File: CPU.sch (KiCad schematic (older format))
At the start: 14 parts, among them J10 SWD, U1 STM32F405RGTx, Y1 8MHz

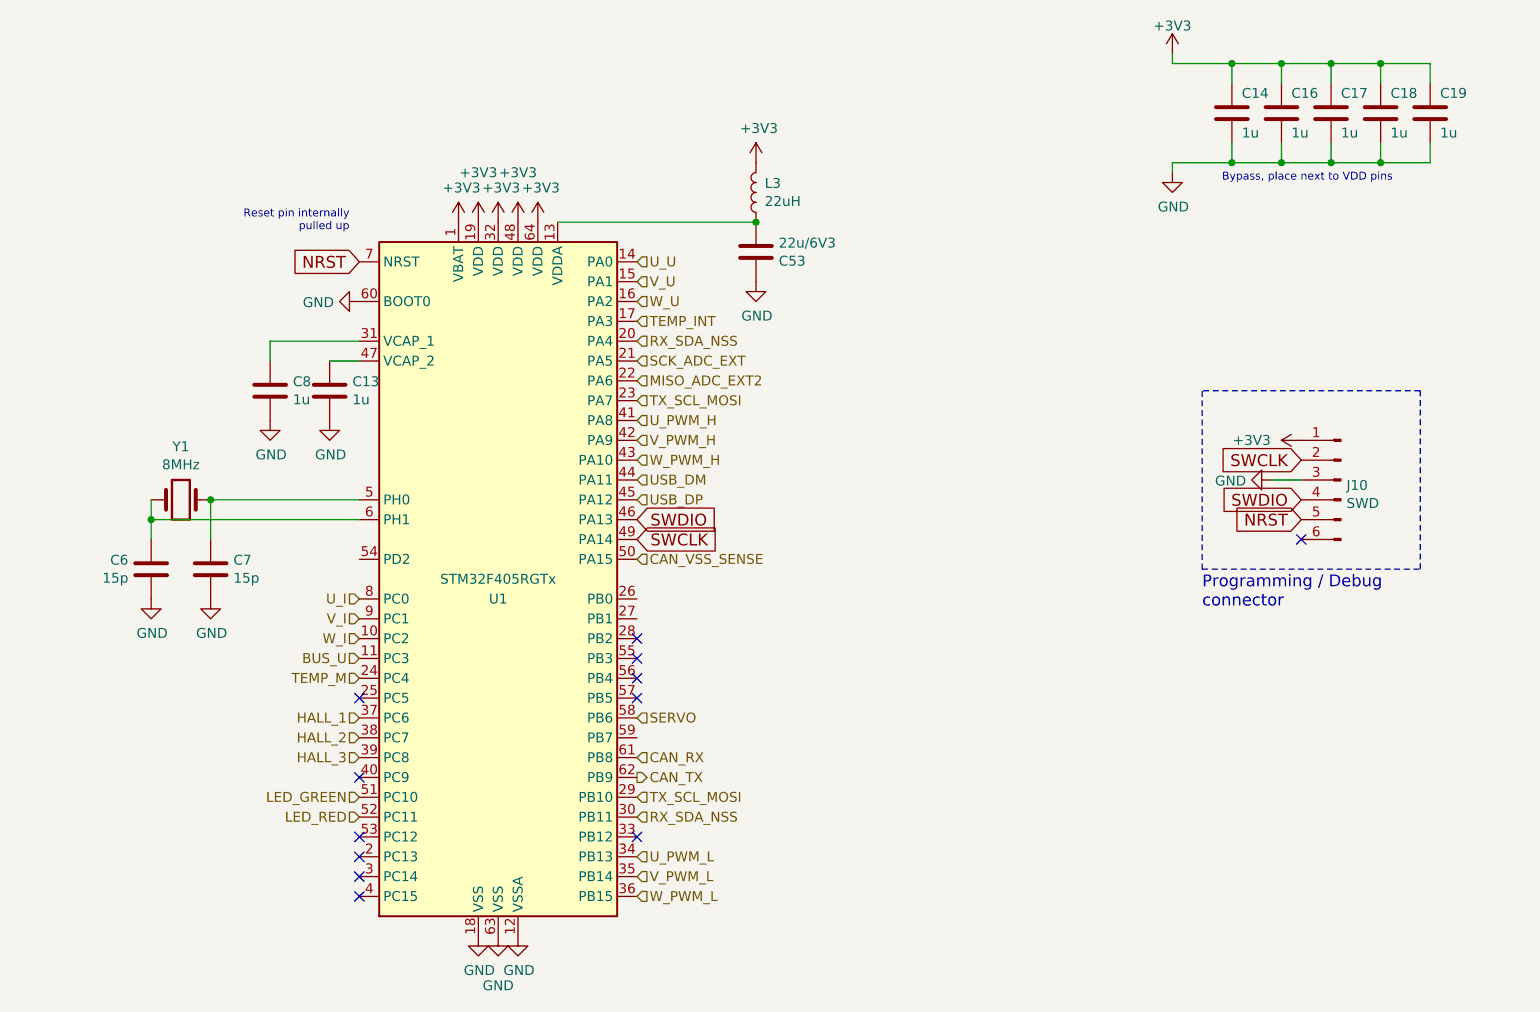
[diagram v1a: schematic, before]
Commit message: - changed CSA for Hall effect sensors - updated power stage layout
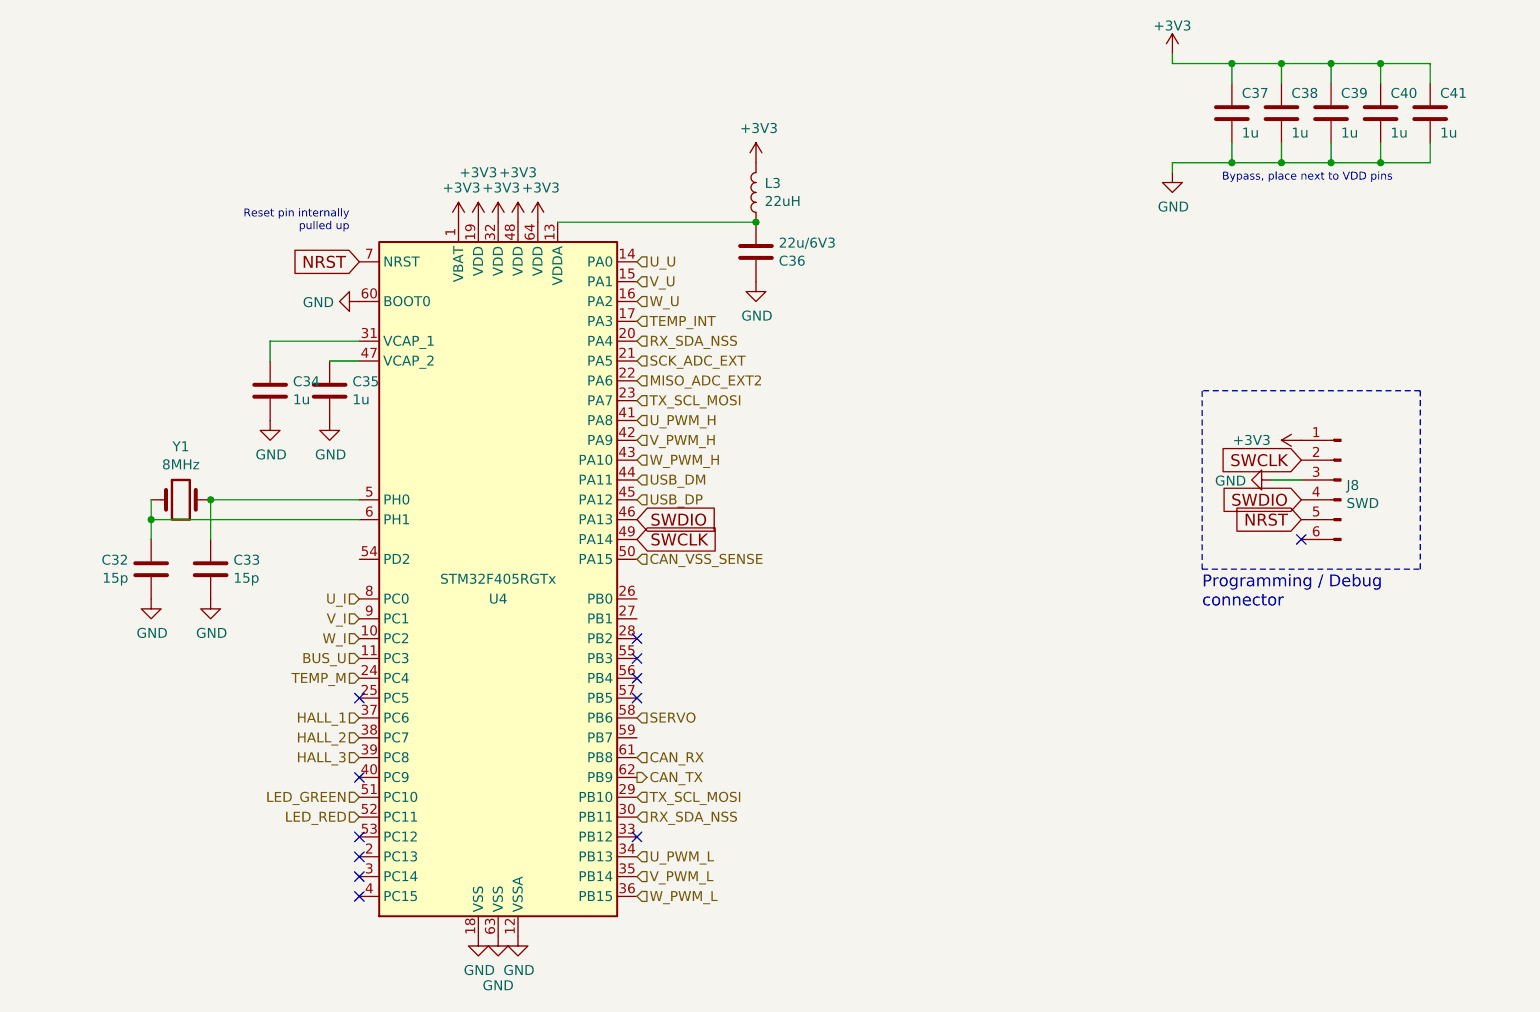
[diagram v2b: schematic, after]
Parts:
- renumbered C6 to C32, C7 to C33, C8 to C34, C13 to C35, C53 to C36, C14 to C37, C16 to C38, C17 to C39, C18 to C40, C19 to C41, J10 to J8, U1 to U4
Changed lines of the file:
@@
 Bypass, place next to VDD pins
 $Comp
-L HSWR-V2-rescue:+3V3-power #PWR050
+L HSWR-V2-rescue:+3V3-power #PWR082
 U 1 1 5752A907
 P 9750 2900
-F 0 "#PWR050" H 9750 2750 50  0001 C CNN
+F 0 "#PWR082" H 9750 2750 50  0001 C CNN
 F 1 "+3V3" V 9750 3150 50  0000 C CNN
 F 2 "" H 9750 2900 50  0000 C CNN
@@
 $EndComp
 $Comp
-L HSWR-V2-rescue:+3V3-power #PWR051
+L HSWR-V2-rescue:+3V3-power #PWR079
 U 1 1 5752A9C6
 P 9100 950
-F 0 "#PWR051" H 9100 800 50  0001 C CNN
+F 0 "#PWR079" H 9100 800 50  0001 C CNN
 F 1 "+3V3" H 9100 1090 50  0000 C CNN
 F 2 "" H 9100 950 50  0000 C CNN
@@
 NoConn ~ 5000 5200
 $Comp
-L HSWR-V2-rescue:C-Device C13
+L HSWR-V2-rescue:C-Device C35
 U 1 1 5CA0C3E8
 P 4850 2650
-F 0 "C13" H 4965 2696 50  0000 L CNN
+F 0 "C35" H 4965 2696 50  0000 L CNN
 F 1 "1u" H 4965 2605 50  0000 L CNN
 F 2 "Capacitor_SMD:C_0805_2012Metric" H 4888 2500 50  0001 C CNN
@@
 $EndComp
 $Comp
-L HSWR-V2-rescue:C-Device C8
+L HSWR-V2-rescue:C-Device C34
 U 1 1 5CA0C416
 P 4550 2650
-F 0 "C8" H 4665 2696 50  0000 L CNN
+F 0 "C34" H 4665 2696 50  0000 L CNN
 F 1 "1u" H 4665 2605 50  0000 L CNN
 F 2 "Capacitor_SMD:C_0805_2012Metric" H 4588 2500 50  0001 C CNN
@@
 	4550 2400 4550 2500
 $Comp
-L HSWR-V2-rescue:GND-power #PWR0123
+L HSWR-V2-rescue:GND-power #PWR066
 U 1 1 5CA0EB5F
 P 4550 2800
-F 0 "#PWR0123" H 4550 2550 50  0001 C CNN
+F 0 "#PWR066" H 4550 2550 50  0001 C CNN
 F 1 "GND" H 4555 2627 50  0000 C CNN
 F 2 "" H 4550 2800 50  0001 C CNN
@@
 $EndComp
 $Comp
-L HSWR-V2-rescue:GND-power #PWR0124
+L HSWR-V2-rescue:GND-power #PWR067
 U 1 1 5CA0EB79
 P 4850 2800
-F 0 "#PWR0124" H 4850 2550 50  0001 C CNN
+F 0 "#PWR067" H 4850 2550 50  0001 C CNN
 F 1 "GND" H 4855 2627 50  0000 C CNN
 F 2 "" H 4850 2800 50  0001 C CNN
@@
 $EndComp
 $Comp
-L HSWR-V2-rescue:GND-power #PWR0125
+L HSWR-V2-rescue:GND-power #PWR068
 U 1 1 5CA0EDF0
 P 5000 2200
-F 0 "#PWR0125" H 5000 1950 50  0001 C CNN
+F 0 "#PWR068" H 5000 1950 50  0001 C CNN
 F 1 "GND" V 5005 2072 50  0000 R CNN
 F 2 "" H 5000 2200 50  0001 C CNN
@@
 $EndComp
 $Comp
-L HSWR-V2-rescue:C-Device C7
+L HSWR-V2-rescue:C-Device C33
 U 1 1 5CA0F099
 P 4250 3550
-F 0 "C7" H 4365 3596 50  0000 L CNN
+F 0 "C33" H 4365 3596 50  0000 L CNN
 F 1 "15p" H 4365 3505 50  0000 L CNN
 F 2 "Capacitor_SMD:C_0805_2012Metric" H 4288 3400 50  0001 C CNN
@@
 $EndComp
 $Comp
-L HSWR-V2-rescue:GND-power #PWR0126
+L HSWR-V2-rescue:GND-power #PWR065
 U 1 1 5CA0F12A
 P 4250 3700
-F 0 "#PWR0126" H 4250 3450 50  0001 C CNN
+F 0 "#PWR065" H 4250 3450 50  0001 C CNN
 F 1 "GND" H 4255 3527 50  0000 C CNN
 F 2 "" H 4250 3700 50  0001 C CNN
@@
 $EndComp
 $Comp
-L HSWR-V2-rescue:C-Device C6
+L HSWR-V2-rescue:C-Device C32
 U 1 1 5CA0F13F
 P 3950 3550
-F 0 "C6" H 3835 3504 50  0000 R CNN
+F 0 "C32" H 3835 3504 50  0000 R CNN
 F 1 "15p" H 3835 3595 50  0000 R CNN
 F 2 "Capacitor_SMD:C_0805_2012Metric" H 3988 3400 50  0001 C CNN
@@
 $EndComp
 $Comp
-L HSWR-V2-rescue:GND-power #PWR0127
+L HSWR-V2-rescue:GND-power #PWR064
 U 1 1 5CA0F180
 P 3950 3700
-F 0 "#PWR0127" H 3950 3450 50  0001 C CNN
+F 0 "#PWR064" H 3950 3450 50  0001 C CNN
 F 1 "GND" H 3955 3527 50  0000 C CNN
 F 2 "" H 3950 3700 50  0001 C CNN
@@
 Connection ~ 4250 3200
 $Comp
-L HSWR-V2-rescue:GND-power #PWR0128
+L HSWR-V2-rescue:GND-power #PWR071
 U 1 1 5CA16A28
 P 5600 5400
-F 0 "#PWR0128" H 5600 5150 50  0001 C CNN
+F 0 "#PWR071" H 5600 5150 50  0001 C CNN
 F 1 "GND" H 5605 5227 50  0000 C CNN
 F 2 "" H 5600 5400 50  0001 C CNN
@@
 $EndComp
 $Comp
-L HSWR-V2-rescue:GND-power #PWR0129
+L HSWR-V2-rescue:GND-power #PWR073
 U 1 1 5CA16A46
 P 5700 5400
-F 0 "#PWR0129" H 5700 5150 50  0001 C CNN
+F 0 "#PWR073" H 5700 5150 50  0001 C CNN
 F 1 "GND" H 5700 5150 50  0000 C CNN
 F 2 "" H 5700 5400 50  0001 C CNN
@@
 $EndComp
 $Comp
-L HSWR-V2-rescue:GND-power #PWR0130
+L HSWR-V2-rescue:GND-power #PWR075
 U 1 1 5CA16A5D
 P 5800 5400
-F 0 "#PWR0130" H 5800 5150 50  0001 C CNN
+F 0 "#PWR075" H 5800 5150 50  0001 C CNN
 F 1 "GND" H 5805 5227 50  0000 C CNN
 F 2 "" H 5800 5400 50  0001 C CNN
@@
 $EndComp
 $Comp
-L HSWR-V2-rescue:+3V3-power #PWR0131
+L HSWR-V2-rescue:+3V3-power #PWR069
 U 1 1 5CA19F46
 P 5500 1800
-F 0 "#PWR0131" H 5500 1650 50  0001 C CNN
+F 0 "#PWR069" H 5500 1650 50  0001 C CNN
 F 1 "+3V3" H 5515 1973 50  0000 C CNN
 F 2 "" H 5500 1800 50  0001 C CNN
@@
 $EndComp
 $Comp
-L HSWR-V2-rescue:+3V3-power #PWR0132
+L HSWR-V2-rescue:+3V3-power #PWR070
 U 1 1 5CA19F6A
 P 5600 1800
-F 0 "#PWR0132" H 5600 1650 50  0001 C CNN
+F 0 "#PWR070" H 5600 1650 50  0001 C CNN
 F 1 "+3V3" H 5600 2050 50  0000 C CNN
 F 2 "" H 5600 1800 50  0001 C CNN
@@
 $EndComp
 $Comp
-L HSWR-V2-rescue:+3V3-power #PWR0133
+L HSWR-V2-rescue:+3V3-power #PWR072
 U 1 1 5CA19F81
 P 5700 1800
-F 0 "#PWR0133" H 5700 1650 50  0001 C CNN
+F 0 "#PWR072" H 5700 1650 50  0001 C CNN
 F 1 "+3V3" H 5715 1973 50  0000 C CNN
 F 2 "" H 5700 1800 50  0001 C CNN
@@
 $EndComp
 $Comp
-L HSWR-V2-rescue:+3V3-power #PWR0134
+L HSWR-V2-rescue:+3V3-power #PWR074
 U 1 1 5CA19F98
 P 5800 1800
-F 0 "#PWR0134" H 5800 1650 50  0001 C CNN
+F 0 "#PWR074" H 5800 1650 50  0001 C CNN
 F 1 "+3V3" H 5800 2050 50  0000 C CNN
 F 2 "" H 5800 1800 50  0001 C CNN
@@
 $EndComp
 $Comp
-L HSWR-V2-rescue:+3V3-power #PWR0135
+L HSWR-V2-rescue:+3V3-power #PWR076
 U 1 1 5CA19FAF
 P 5900 1800
-F 0 "#PWR0135" H 5900 1650 50  0001 C CNN
+F 0 "#PWR076" H 5900 1650 50  0001 C CNN
 F 1 "+3V3" H 5915 1973 50  0000 C CNN
 F 2 "" H 5900 1800 50  0001 C CNN
@@
 $EndComp
 $Comp
-L HSWR-V2-rescue:GND-power #PWR0137
+L HSWR-V2-rescue:GND-power #PWR080
 U 1 1 5CA1AE02
 P 9100 1550
-F 0 "#PWR0137" H 9100 1300 50  0001 C CNN
+F 0 "#PWR080" H 9100 1300 50  0001 C CNN
 F 1 "GND" H 9105 1377 50  0000 C CNN
 F 2 "" H 9100 1550 50  0001 C CNN
@@
 $EndComp
 $Comp
-L HSWR-V2-rescue:C-Device C14
+L HSWR-V2-rescue:C-Device C37
 U 1 1 5CA1AE66
 P 9400 1250
-F 0 "C14" H 9450 1350 50  0000 L CNN
+F 0 "C37" H 9450 1350 50  0000 L CNN
 F 1 "1u" H 9450 1150 50  0000 L CNN
 F 2 "Capacitor_SMD:C_0805_2012Metric" H 9438 1100 50  0001 C CNN
@@
 $EndComp
 $Comp
-L HSWR-V2-rescue:C-Device C16
+L HSWR-V2-rescue:C-Device C38
 U 1 1 5CA1B11D
 P 9650 1250
-F 0 "C16" H 9700 1350 50  0000 L CNN
+F 0 "C38" H 9700 1350 50  0000 L CNN
 F 1 "1u" H 9700 1150 50  0000 L CNN
 F 2 "Capacitor_SMD:C_0805_2012Metric" H 9688 1100 50  0001 C CNN
@@
 $EndComp
 $Comp
-L HSWR-V2-rescue:C-Device C17
+L HSWR-V2-rescue:C-Device C39
 U 1 1 5CA1B141
 P 9900 1250
-F 0 "C17" H 9950 1350 50  0000 L CNN
+F 0 "C39" H 9950 1350 50  0000 L CNN
 F 1 "1u" H 9950 1150 50  0000 L CNN
 F 2 "Capacitor_SMD:C_0805_2012Metric" H 9938 1100 50  0001 C CNN
@@
 	9900 1000 10150 1000
 $Comp
-L HSWR-V2-rescue:C-Device C18
+L HSWR-V2-rescue:C-Device C40
 U 1 1 5CA1B849
 P 10150 1250
-F 0 "C18" H 10200 1350 50  0000 L CNN
+F 0 "C40" H 10200 1350 50  0000 L CNN
 F 1 "1u" H 10200 1150 50  0000 L CNN
 F 2 "Capacitor_SMD:C_0805_2012Metric" H 10188 1100 50  0001 C CNN
@@
 	10150 1000 10400 1000
 $Comp
-L HSWR-V2-rescue:C-Device C19
+L HSWR-V2-rescue:C-Device C41
 U 1 1 5CA1BC9F
 P 10400 1250
-F 0 "C19" H 10450 1350 50  0000 L CNN
+F 0 "C41" H 10450 1350 50  0000 L CNN
 F 1 "1u" H 10450 1150 50  0000 L CNN
 F 2 "Capacitor_SMD:C_0805_2012Metric" H 10438 1100 50  0001 C CNN
@@
 Connection ~ 10150 1500
 $Comp
-L HSWR-V2-rescue:Conn_01x06_Male-Connector J10
+L HSWR-V2-rescue:Conn_01x06_Male-Connector J8
 U 1 1 5CA1C65D
 P 9950 3100
-F 0 "J10" H 9922 3073 50  0000 R CNN
+F 0 "J8" H 9922 3073 50  0000 R CNN
 F 1 "SWD" H 9922 2982 50  0000 R CNN
 F 2 "Connector_PinHeader_2.54mm:PinHeader_2x03_P2.54mm_Vertical" H 9950 3100 50  0001 C CNN
@@
 $EndComp
 $Comp
-L HSWR-V2-rescue:GND-power #PWR0138
+L HSWR-V2-rescue:GND-power #PWR081
 U 1 1 5CA1C964
 P 9600 3100
-F 0 "#PWR0138" H 9600 2850 50  0001 C CNN
+F 0 "#PWR081" H 9600 2850 50  0001 C CNN
 F 1 "GND" V 9605 2972 50  0000 R CNN
 F 2 "" H 9600 3100 50  0001 C CNN
@@
 $EndComp
 $Comp
-L HSWR-V2-rescue:STM32F405RGTx-MCU_ST_STM32F4 U1
+L HSWR-V2-rescue:STM32F405RGTx-MCU_ST_STM32F4 U4
 U 1 1 5C9EF5EF
 P 5700 3600
-F 0 "U1" H 5700 3500 50  0000 C CNN
+F 0 "U4" H 5700 3500 50  0000 C CNN
 F 1 "STM32F405RGTx" H 5700 3600 50  0000 C CNN
 F 2 "Package_QFP:LQFP-64_10x10mm_P0.5mm" H 5100 1900 50  0001 R CNN
@@
 CAN_VSS_SENSE
 $Comp
-L HSWR-V2-rescue:+3V3-power #PWR0136
+L HSWR-V2-rescue:+3V3-power #PWR077
 U 1 1 5E23B21C
 P 7000 1500
-F 0 "#PWR0136" H 7000 1350 50  0001 C CNN
+F 0 "#PWR077" H 7000 1350 50  0001 C CNN
 F 1 "+3V3" H 7015 1673 50  0000 C CNN
 F 2 "" H 7000 1500 50  0001 C CNN
@@
 $EndComp
 $Comp
-L HSWR-V2-rescue:C-Device C53
+L HSWR-V2-rescue:C-Device C36
 U 1 1 5E23CCCB
 P 7000 1950
-F 0 "C53" H 7115 1996 50  0000 L CNN
+F 0 "C36" H 7115 1996 50  0000 L CNN
 F 1 "22u/6V3" H 7115 1905 50  0000 L CNN
 F 2 "Capacitor_SMD:C_0805_2012Metric" H 7038 1800 50  0001 C CNN
@@
 $EndComp
 $Comp
-L HSWR-V2-rescue:GND-power #PWR0177
+L HSWR-V2-rescue:GND-power #PWR078
 U 1 1 5E23DDB0
 P 7000 2100
-F 0 "#PWR0177" H 7000 1850 50  0001 C CNN
+F 0 "#PWR078" H 7000 1850 50  0001 C CNN
 F 1 "GND" H 7005 1927 50  0000 C CNN
 F 2 "" H 7000 2100 50  0001 C CNN

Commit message: - removed rescue lib and symbols - added HSWR.lib
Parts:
- C32, C33, C34, C35, C36, C37, C38, C39, C40, C41: symbol HSWR-V2-rescue:C-Device -> Device:C
- J8: symbol HSWR-V2-rescue:Conn_01x06_Male-Connector -> Connector:Conn_01x06_Male
- U4: symbol HSWR-V2-rescue:STM32F405RGTx-MCU_ST_STM32F4 -> MCU_ST_STM32F4:STM32F405RGTx
- Y1: symbol HSWR-V2-rescue:Crystal-Device -> Device:Crystal
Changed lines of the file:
@@
 Bypass, place next to VDD pins
 $Comp
-L HSWR-V2-rescue:+3V3-power #PWR082
+L power:+3V3 #PWR082
 U 1 1 5752A907
 P 9750 2900
@@
 $EndComp
 $Comp
-L HSWR-V2-rescue:+3V3-power #PWR079
+L power:+3V3 #PWR079
 U 1 1 5752A9C6
 P 9100 950
@@
 	9650 1000 9900 1000
 $Comp
-L HSWR-V2-rescue:Crystal-Device Y1
+L Device:Crystal Y1
 U 1 1 5B6893E1
 P 4100 3200
@@
 NoConn ~ 5000 5200
 $Comp
-L HSWR-V2-rescue:C-Device C35
+L Device:C C35
 U 1 1 5CA0C3E8
 P 4850 2650
@@
 $EndComp
 $Comp
-L HSWR-V2-rescue:C-Device C34
+L Device:C C34
 U 1 1 5CA0C416
 P 4550 2650
@@
 	5000 2500 4850 2500
 Wire Wire Line
-	5000 2400 4550 2400
+	5000 2400 4800 2400
 Wire Wire Line
 	4550 2400 4550 2500
 $Comp
-L HSWR-V2-rescue:GND-power #PWR066
+L power:GND #PWR066
 U 1 1 5CA0EB5F
 P 4550 2800
@@
 $EndComp
 $Comp
-L HSWR-V2-rescue:GND-power #PWR067
-U 1 1 5CA0EB79
-P 4850 2800
-F 0 "#PWR067" H 4850 2550 50  0001 C CNN
-F 1 "GND" H 4855 2627 50  0000 C CNN
-F 2 "" H 4850 2800 50  0001 C CNN
-F 3 "" H 4850 2800 50  0001 C CNN
-	1    4850 2800
-	1    0    0    -1
-$EndComp
-$Comp
-L HSWR-V2-rescue:GND-power #PWR068
+L power:GND #PWR068
 U 1 1 5CA0EDF0
 P 5000 2200
@@
 $EndComp
 $Comp
-L HSWR-V2-rescue:C-Device C33
+L Device:C C33
 U 1 1 5CA0F099
 P 4250 3550
@@
 $EndComp
 $Comp
-L HSWR-V2-rescue:GND-power #PWR065
+L power:GND #PWR065
 U 1 1 5CA0F12A
 P 4250 3700
@@
 $EndComp
 $Comp
-L HSWR-V2-rescue:C-Device C32
+L Device:C C32
 U 1 1 5CA0F13F
 P 3950 3550
@@
 $EndComp
 $Comp
-L HSWR-V2-rescue:GND-power #PWR064
+L power:GND #PWR064
 U 1 1 5CA0F180
 P 3950 3700
@@
 Wire Wire Line
 	4250 3400 4250 3200
-Connection ~ 4250 3200
-$Comp
-L HSWR-V2-rescue:GND-power #PWR071
+$Comp
+L power:GND #PWR071
 U 1 1 5CA16A28
 P 5600 5400
@@
 $EndComp
 $Comp
-L HSWR-V2-rescue:GND-power #PWR073
+L power:GND #PWR073
 U 1 1 5CA16A46
 P 5700 5400
@@
 $EndComp
 $Comp
-L HSWR-V2-rescue:GND-power #PWR075
+L power:GND #PWR075
 U 1 1 5CA16A5D
 P 5800 5400
@@
 $EndComp
 $Comp
-L HSWR-V2-rescue:+3V3-power #PWR069
+L power:+3V3 #PWR069
 U 1 1 5CA19F46
 P 5500 1800
@@
 $EndComp
 $Comp
-L HSWR-V2-rescue:+3V3-power #PWR070
+L power:+3V3 #PWR070
 U 1 1 5CA19F6A
 P 5600 1800
@@
 $EndComp
 $Comp
-L HSWR-V2-rescue:+3V3-power #PWR072
+L power:+3V3 #PWR072
 U 1 1 5CA19F81
 P 5700 1800
@@
 $EndComp
 $Comp
-L HSWR-V2-rescue:+3V3-power #PWR074
+L power:+3V3 #PWR074
 U 1 1 5CA19F98
 P 5800 1800
@@
 $EndComp
 $Comp
-L HSWR-V2-rescue:+3V3-power #PWR076
+L power:+3V3 #PWR076
 U 1 1 5CA19FAF
 P 5900 1800
@@
 $EndComp
 $Comp
-L HSWR-V2-rescue:GND-power #PWR080
+L power:GND #PWR080
 U 1 1 5CA1AE02
 P 9100 1550
@@
 $EndComp
 $Comp
-L HSWR-V2-rescue:C-Device C37
+L Device:C C37
 U 1 1 5CA1AE66
 P 9400 1250
@@
 $EndComp
 $Comp
-L HSWR-V2-rescue:C-Device C38
+L Device:C C38
 U 1 1 5CA1B11D
 P 9650 1250
@@
 $EndComp
 $Comp
-L HSWR-V2-rescue:C-Device C39
+L Device:C C39
 U 1 1 5CA1B141
 P 9900 1250
@@
 	9900 1000 10150 1000
 $Comp
-L HSWR-V2-rescue:C-Device C40
+L Device:C C40
 U 1 1 5CA1B849
 P 10150 1250
@@
 	10150 1000 10400 1000
 $Comp
-L HSWR-V2-rescue:C-Device C41
+L Device:C C41
 U 1 1 5CA1BC9F
 P 10400 1250
@@
 Connection ~ 10150 1500
 $Comp
-L HSWR-V2-rescue:Conn_01x06_Male-Connector J8
+L Connector:Conn_01x06_Male J8
 U 1 1 5CA1C65D
 P 9950 3100
@@
 $EndComp
 $Comp
-L HSWR-V2-rescue:GND-power #PWR081
+L power:GND #PWR081
 U 1 1 5CA1C964
 P 9600 3100
@@
 $EndComp
 $Comp
-L HSWR-V2-rescue:STM32F405RGTx-MCU_ST_STM32F4 U4
+L MCU_ST_STM32F4:STM32F405RGTx U4
 U 1 1 5C9EF5EF
 P 5700 3600
@@
 CAN_VSS_SENSE
 $Comp
-L HSWR-V2-rescue:+3V3-power #PWR077
+L power:+3V3 #PWR077
 U 1 1 5E23B21C
 P 7000 1500
@@
 $EndComp
 $Comp
-L HSWR-V2-rescue:C-Device C36
+L Device:C C36
 U 1 1 5E23CCCB
 P 7000 1950
@@
 $EndComp
 $Comp
-L HSWR-V2-rescue:GND-power #PWR078
+L power:GND #PWR078
 U 1 1 5E23DDB0
 P 7000 2100
@@
 	1    0    0    -1
 $EndComp
+Wire Wire Line
+	6000 1800 7000 1800
+Wire Wire Line
+	9400 1000 9650 1000
+Wire Wire Line
+	9400 1500 9650 1500
+$Comp
+L power:GND #PWR067
+U 1 1 5CA0EB79
+P 4850 2800
+F 0 "#PWR067" H 4850 2550 50  0001 C CNN
+F 1 "GND" H 4855 2627 50  0000 C CNN
+F 2 "" H 4850 2800 50  0001 C CNN
+F 3 "" H 4850 2800 50  0001 C CNN
+	1    4850 2800
+	1    0    0    -1
+$EndComp
+Connection ~ 4250 3200
+Connection ~ 4800 2400
+Wire Wire Line
+	4800 2400 4550 2400
 Connection ~ 7000 1800
-Wire Wire Line
-	6000 1800 7000 1800
-Wire Wire Line
-	9400 1000 9650 1000
-Wire Wire Line
-	9400 1500 9650 1500
 $EndSCHEMATC
